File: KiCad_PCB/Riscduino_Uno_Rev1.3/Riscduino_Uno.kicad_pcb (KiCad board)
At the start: 2 copper layers, 68.8 x 53.6 mm, 87 parts, among them J10 Conn_01x06_Pin, J11 USB_B_Micro, J12 Conn_01x08_Pin, J13 Conn_01x10_Pin, J2 Conn_01x03_Pin, J3 Conn_01x01, J4 Conn_02x04_Odd_Even, J5 ISP, J6 Conn_01x01, J7 Conn_01x01, J8 Conn_01x01, J9 Conn_01x08_Pin, SW1 4Pin Round Button SPST Straig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, U2 W25Q32JVSS, U3 23LC1024-I/P, U4 W25Q32JVSS, U5 Riscduino, U6 LM1117MP-3.3, U7 LM1117S-ADJ, U8 CH340C, X1 ASE-10.000MHZ-LC-T

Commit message: Update
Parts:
- added R19: 0E, Riscduino:R_0603_1608Metric_Pad0.98x0.95mm_HandSolder, B.Cu at (119.2, 88.7)
- added R25: 0E, Riscduino:R_0603_1608Metric_Pad0.98x0.95mm_HandSolder, B.Cu at (119.2, 90.2)
- C15: moved to B.Cu
- C16: renamed from C17; moved to B.Cu
- C17: renamed from C18; moved to B.Cu
- C23: renamed from C10; moved to B.Cu
- C24: renamed from C12; moved to B.Cu
- R13: renamed from R14; moved to B.Cu
- R26: renamed from R15; moved to B.Cu
- R27: renamed from R16; moved to B.Cu
- moved R15 21.8 mm to (111.7, 59.6)
- moved C3 21.7 mm to (133.9, 50.8), turned to 180 degrees
- moved D2 19.0 mm to (111.5, 61.4), turned to 180 degrees
- moved J7 16.1 mm to (122.7, 66.6), turned to 90 degrees
- moved C20 14.5 mm to (135.1, 66.5), turned to 90 degrees
- moved C15 12.6 mm to (132.9, 66.5), turned to 90 degrees
- moved C26 11.5 mm to (130.2, 93.9)
- moved JP2 9.30 mm to (124.3, 75.0)
- moved C25 8.30 mm to (130.1, 90.2), turned to -90 degrees
- moved R24 8.06 mm to (119.2, 94.0), turned to 180 degrees
- moved C17 5.29 mm to (126.4, 65.2), turned to 180 degrees
- moved U5 4.21 mm to (125.0, 88.0)
- moved J5 3.85 mm to (117.9, 61.8)
- moved J4 3.53 mm to (118.1, 57.8)
- moved R12 3.47 mm to (127.3, 55.8), turned to 90 degrees
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- renumbered C6 to C10, C8 to C11, C14 to C12, C16 to C13, C19 to C14, C22 to C18, C21 to C19, C23 to C20, C24 to C21, C25 to C22, C20 to C25, C7 to C5, C9 to C6, C11 to C7, C13 to C8, C5 to C9, D3 to D2, D1 to D3, J5 to J1, J13 to J10, J2 to J11, J7 to J12, J10 to J2, J9 to J3, J6 to J4, J3 to J5, J4 to J6, J8 to J7, J11 to J8, J12 to J9, JP2 to JP1, JP1 to JP2, R2 to R1, R12 to R10, R5 to R11, R32 to R12, R19 to R14, R23 to R15, R20 to R16, R21 to R17, R22 to R18, R4 to R2, R25 to R20, R27 to R21, R29 to R22, R28 to R23, R33 to R24, R24 to R28, R26 to R29, R6 to R3, R7 to R4, R3 to R5, R9 to R6, R8 to R7, R13 to R8, R11 to R9, U4 to U1, U3 to U2, U5 to U3, U6 to U4, U8 to U5, U7 to U6, U2 to U7
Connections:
- J10 pad 8: mprj_io_12 -> mprj_io_30
- U5 pad 2: ardunio_d0 -> Net-(U5-TXD)
- U5 pad 3: ardunio_d1 -> Net-(U5-RXD)
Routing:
- net ardunio_d3: track 124.0 -> 63.5 mm, vias 5 -> 1
- net mprj_io_12: track 87.0 -> 35.3 mm, vias 5 -> 3
- net ardunio_d2: track 120.7 -> 70.1 mm, vias 5 -> 1
- net +3.3V: track 358.2 -> 397.8 mm, vias 14 -> 8
- net CARAVEL_FLASH_IO0: track 81.9 -> 112.5 mm
- net ardunio_d4: track 84.9 -> 55.2 mm, vias 2 -> 1
- net mprj_io_30: track 0.00 -> 27.8 mm, vias 0 -> 2
- net ardunio_d0: track 102.1 -> 79.3 mm, vias 6 -> 2
- net USER_SRAM_SSN: track 88.2 -> 65.7 mm, vias 3 -> 4
- net USER_FLASH_IO2: track 80.3 -> 99.7 mm, vias 2 -> 3
- net +5VP: track 13.9 -> 33.2 mm, vias 1 -> 0
- net Net-(U6-ADJ): track 14.4 -> 33.1 mm
- net ardunio_a1: track 71.4 -> 53.3 mm, vias 6 -> 1
- net USER_FLASH_IO3: track 100.6 -> 118.3 mm, vias 4 -> 3
- net ISP_SSN: track 64.8 -> 48.5 mm, vias 3 -> 0
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
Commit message: Power Supervisory Circuit
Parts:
- added C28: 0.1uf, Riscduino.Library:C_0603_1608Metric_Pad1.08x0.95mm_HandSolder, B.Cu at (128.3, 51.7)
- added U8: APX811, Package_TO_SOT_SMD:SOT-143_Handsoldering, B.Cu at (133.1, 51.8)
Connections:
- C3 pad 1: ~{RST} -> ~{MR}
- R1 pad 2: ~{RST} -> ~{MR}
- R12 pad 2: ~{RST} -> ~{MR}
- SW1 pad 2: ~{RST} -> ~{MR}
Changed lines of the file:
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@@
   (net 82 "unconnected-(U5-~{RTS}-Pad14)")
   (net 83 "unconnected-(U5-R232-Pad15)")
+  (net 84 "~{MR}")
   (footprint "Connector_PinHeader_2.54mm:PinHeader_1x01_P2.54mm_Vertical" (layer "F.Cu")
     (at 118.1354 57.8358 180)
@@
       (net 4 "+3.3V") (pintype "passive"))
     (pad "2" smd roundrect (at 0.9125 0) (size 1.1 0.95) (layers "F.Cu" "F.Paste" "F.Mask") (roundrect_rratio 0.25)
-      (net 14 "~{RST}") (pintype "passive"))
+      (net 84 "~{MR}") (pintype "passive"))
     (model "${KICAD6_3DMODEL_DIR}/Resistor_SMD.3dshapes/R_0603_1608Metric.wrl"
       (offset (xyz 0 0 0))
@@
       (stroke (width 0.1) (type solid)) (layer "F.Fab"))
     (pad "1" smd roundrect (at -1.0375 0 180) (size 1.175 1.45) (layers "F.Cu" "F.Paste" "F.Mask") (roundrect_rratio 0.2127659574)
-      (net 14 "~{RST}") (pintype "passive"))
+      (net 84 "~{MR}") (pintype "passive"))
     (pad "2" smd roundrect (at 1.0375 0 180) (size 1.175 1.45) (layers "F.Cu" "F.Paste" "F.Mask") (roundrect_rratio 0.2127659574)
       (net 2 "GND") (pintype "passive"))
@@
       (net 2 "GND") (pinfunction "1") (pintype "passive"))
     (pad "2" smd rect (at -2.88 2 180) (size 2.75 1) (layers "F.Cu" "F.Paste" "F.Mask")
-      (net 14 "~{RST}") (pinfunction "2") (pintype "passive"))
+      (net 84 "~{MR}") (pinfunction "2") (pintype "passive"))
     (pad "2" smd rect (at 2.88 2 180) (size 2.75 1) (layers "F.Cu" "F.Paste" "F.Mask")
-      (net 14 "~{RST}") (pinfunction "2") (pintype "passive"))
+      (net 84 "~{MR}") (pinfunction "2") (pintype "passive"))
     (model "${KICAD6_3DMODEL_DIR}/Button_Switch_SMD.3dshapes/SW_SPST_EVPBF.wrl"
       (offset (xyz 0 0 0))
@@
       (net 80 "Net-(C26-Pad2)") (pintype "passive"))
     (pad "2" smd roundrect (at 0.9125 0 90) (size 1.1 0.95) (layers "B.Cu" "B.Paste" "B.Mask") (roundrect_rratio 0.25)
-      (net 14 "~{RST}") (pintype "passive"))
+      (net 84 "~{MR}") (pintype "passive"))
     (model "${KICAD6_3DMODEL_DIR}/Resistor_SMD.3dshapes/R_0603_1608Metric.wrl"
       (offset (xyz 0 0 0))
@@
     )
   )
+  (footprint "Riscduino.Library:C_0603_1608Metric_Pad1.08x0.95mm_HandSolder" (layer "B.Cu")
+    (at 128.27 51.6625 -90)
+    (descr "Capacitor SMD 0603 (1608 Metric), square (rectangular) end terminal, IPC_7351 nominal with elongated pad for handsoldering. (Body size source: IPC-SM-782 page 76, https://www.pcb-3d.com/wordpress/wp-content/uploads/ipc-sm-782a_amendment_1_and_2.pdf), generated with kicad-footprint-generator")
+    (tags "capacitor handsolder")
+    (property "Sheetfile" "Riscduino_Uno.kicad_sch")
+    (property "Sheetname" "")
+    (property "ki_description" "Unpolarized capacitor")
+    (property "ki_keywords" "cap capacitor")
+    (attr smd)
+    (fp_text reference "C28" (at -0.2036 -1.2446 90) (layer "B.SilkS")
+        (effects (font (size 1.016 1.016) (thickness 0.1524)) (justify mirror))
+    )
+    (fp_text value "0.1uf" (at 0 -1.43 90) (layer "B.Fab") hide
+        (effects (font (size 1 1) (thickness 0.15)) (justify mirror))
+    )
+    (fp_text user "${REFERENCE}" (at 0 0 90) (layer "B.Fab") hide
+        (effects (font (size 0.4 0.4) (thickness 0.06)) (justify mirror))
+    )
+    (fp_line (start -0.146267 -0.51) (end 0.146267 -0.51)
+      (stroke (width 0.12) (type solid)) (layer "B.SilkS"))
+    (fp_line (start -0.146267 0.51) (end 0.146267 0.51)
+      (stroke (width 0.12) (type solid)) (layer "B.SilkS"))
+    (fp_line (start -1.65 -0.73) (end -1.65 0.73)
+      (stroke (width 0.05) (type solid)) (layer "B.CrtYd"))
+    (fp_line (start -1.65 0.73) (end 1.65 0.73)
+      (stroke (width 0.05) (type solid)) (layer "B.CrtYd"))
+    (fp_line (start 1.65 -0.73) (end -1.65 -0.73)
+      (stroke (width 0.05) (type solid)) (layer "B.CrtYd"))
+    (fp_line (start 1.65 0.73) (end 1.65 -0.73)
+      (stroke (width 0.05) (type solid)) (layer "B.CrtYd"))
+    (fp_line (start -0.8 -0.4) (end -0.8 0.4)
+      (stroke (width 0.1) (type solid)) (layer "B.Fab"))
+    (fp_line (start -0.8 0.4) (end 0.8 0.4)
+      (stroke (width 0.1) (type solid)) (layer "B.Fab"))
+    (fp_line (start 0.8 -0.4) (end -0.8 -0.4)
+      (stroke (width 0.1) (type solid)) (layer "B.Fab"))
+    (fp_line (start 0.8 0.4) (end 0.8 -0.4)
+      (stroke (width 0.1) (type solid)) (layer "B.Fab"))
+    (pad "1" smd roundrect (at -0.8625 0 270) (size 1.075 0.95) (layers "B.Cu" "B.Paste" "B.Mask") (roundrect_rratio 0.25)
+      (net 4 "+3.3V") (pintype "passive"))
+    (pad "2" smd roundrect (at 0.8625 0 270) (size 1.075 0.95) (layers "B.Cu" "B.Paste" "B.Mask") (roundrect_rratio 0.25)
+      (net 2 "GND") (pintype "passive"))
+    (model "${KICAD6_3DMODEL_DIR}/Capacitor_SMD.3dshapes/C_0603_1608Metric.wrl"
+      (offset (xyz 0 0 0))
+      (scale (xyz 1 1 1))
+      (rotate (xyz 0 0 0))
+    )
+  )
   (footprint "Riscduino.Library:R_0603_1608Metric_Pad0.98x0.95mm_HandSolder" (layer "B.Cu")
     (at 87.3252 85.2189 -90)
@@
       (offset (xyz 0 0 0))
       (scale (xyz 1 1 1))
+      (rotate (xyz 0 0 0))
+    )
+  )
+  (footprint "Package_TO_SOT_SMD:SOT-143_Handsoldering" (layer "B.Cu")
+    (at 133.096 51.816 180)
+    (descr "SOT-143 Handsoldering https://www.nxp.com/docs/en/package-information/SOT143B.pdf")
+    (tags "SOT-143 Handsoldering")
+    (property "Sheetfile" "Riscduino_Uno.kicad_sch")
+    (property "Sheetname" "")
+    (property "ki_description" "Power supply supervisor, Manual reset, Threshold 3.08V, SOT-143")
+    (property "ki_keywords" "Supervisor Reset")
+    (attr smd)
+    (fp_text reference "U8" (at -3.556 0 90) (layer "B.SilkS")
+        (effects (font (size 1 1) (thickness 0.15)) (justify mirror))
+    )
+    (fp_text value "APX811" (at -0.02 -2.48) (layer "B.Fab")
+        (effects (font (size 1 1) (thickness 0.15)) (justify mirror))
+    )
+    (fp_text user "${REFERENCE}" (at 0 0 90) (layer "B.Fab")
+        (effects (font (size 0.5 0.5) (thickness 0.075)) (justify mirror))
+    )
+    (fp_line (start -0.65 -1.56) (end 0.65 -1.56)
+      (stroke (width 0.12) (type solid)) (layer "B.SilkS"))
+    (fp_line (start 0.65 1.56) (end -2.35 1.56)
+      (stroke (width 0.12) (type solid)) (layer "B.SilkS"))
+    (fp_line (start -2.6 -1.7) (end -2.6 1.7)
+      (stroke (width 0.05) (type solid)) (layer "B.CrtYd"))
+    (fp_line (start -2.6 -1.7) (end 2.6 -1.7)
+      (stroke (width 0.05) (type solid)) (layer "B.CrtYd"))
+    (fp_line (start 2.6 1.7) (end -2.6 1.7)
+      (stroke (width 0.05) (type solid)) (layer "B.CrtYd"))
+    (fp_line (start 2.6 1.7) (end 2.6 -1.7)
+      (stroke (width 0.05) (type solid)) (layer "B.CrtYd"))
+    (fp_line (start -0.65 -1.45) (end -0.65 0.95)
+      (stroke (width 0.1) (type solid)) (layer "B.Fab"))
+    (fp_line (start -0.65 0.95) (end -0.15 1.45)
+      (stroke (width 0.1) (type solid)) (layer "B.Fab"))
+    (fp_line (start -0.15 1.45) (end 0.65 1.45)
+      (stroke (width 0.1) (type solid)) (layer "B.Fab"))
+    (fp_line (start 0.65 -1.45) (end -0.65 -1.45)
+      (stroke (width 0.1) (type solid)) (layer "B.Fab"))
+    (fp_line (start 0.65 1.45) (end 0.65 -1.45)
+      (stroke (width 0.1) (type solid)) (layer "B.Fab"))
+    (pad "1" smd rect (at -1.5 0.75 180) (size 1.7 1) (layers "B.Cu" "B.Paste" "B.Mask")
+      (net 2 "GND") (pinfunction "GND") (pintype "power_in"))
+    (pad "2" smd rect (at -1.5 -0.95 180) (size 1.7 0.6) (layers "B.Cu" "B.Paste" "B.Mask")
+      (net 14 "~{RST}") (pinfunction "~{RESET}") (pintype "output"))
+    (pad "3" smd rect (at 1.5 -0.95 180) (size 1.7 0.6) (layers "B.Cu" "B.Paste" "B.Mask")
+      (net 84 "~{MR}") (pinfunction "~{MR}") (pintype "input"))
+    (pad "4" smd rect (at 1.5 0.95 180) (size 1.7 0.6) (layers "B.Cu" "B.Paste" "B.Mask")
+      (net 4 "+3.3V") (pinfunction "VCC") (pintype "power_in"))
+    (model "${KICAD6_3DMODEL_DIR}/Package_TO_SOT_SMD.3dshapes/SOT-143.wrl"
+      (offset (xyz 0 0 0))
+      (scale (xyz 1 1 1))

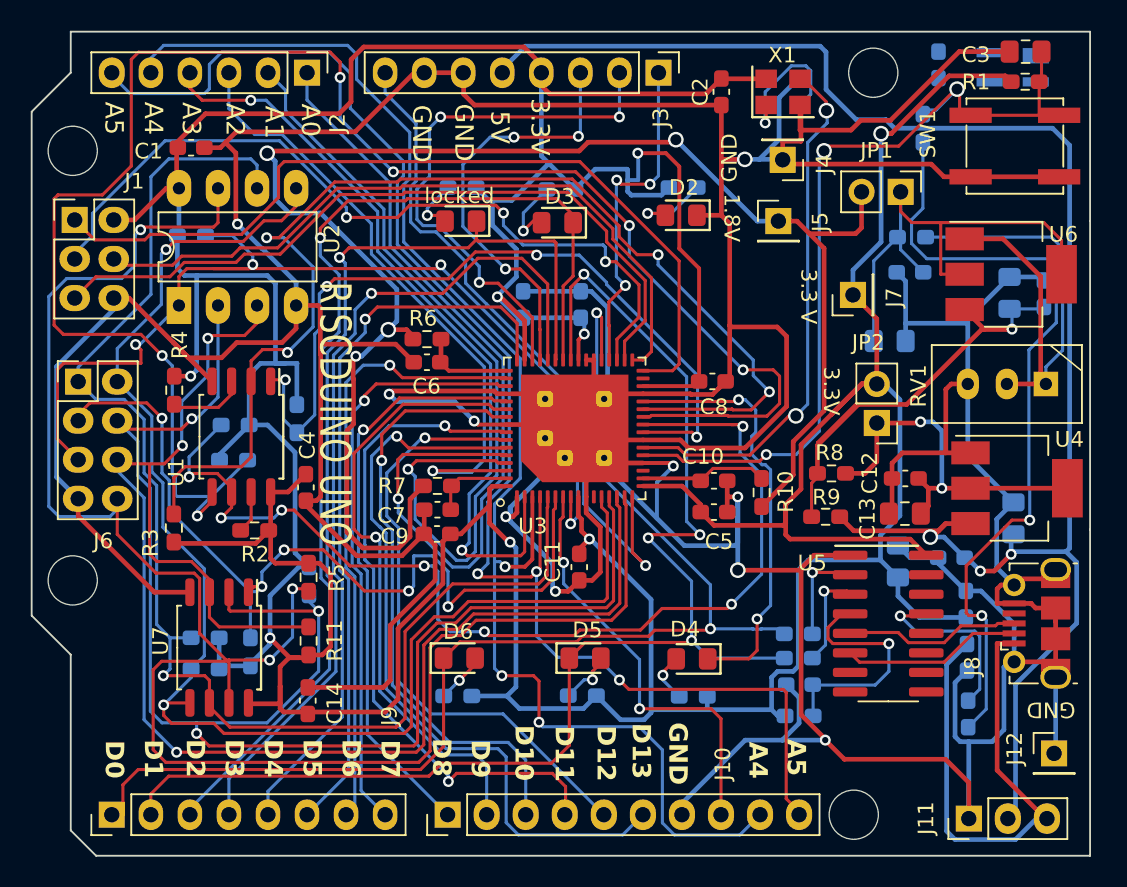
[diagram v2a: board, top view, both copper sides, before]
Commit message: 1.3 Uno Schematic update
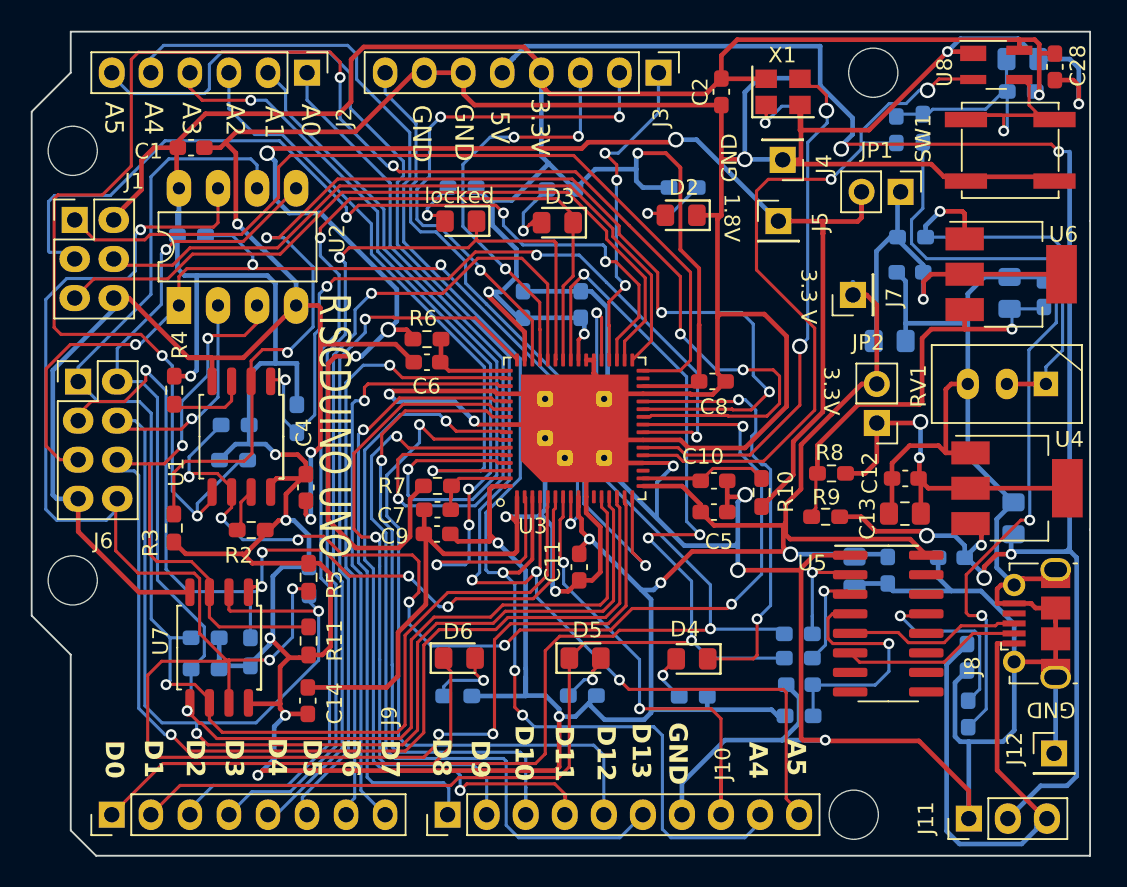
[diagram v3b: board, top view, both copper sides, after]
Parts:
- added R32: 0E-DNI, Riscduino:C_0603_1608Metric_Pad1.08x0.95mm_HandSolder, B.Cu at (125.5, 55.9)
- C28: moved to F.Cu
- C3, R1: moved to B.Cu
- U8: value APX811 -> APX811-29UG-7; moved to F.Cu
- moved C28 7.57 mm to (135.8, 51.8)
- moved C22 5.54 mm to (125.0, 84.5), turned to -90 degrees
- moved C16 2.91 mm to (122.8, 84.7), turned to -90 degrees
- moved U8 1.08 mm to (132.0, 51.7), turned to 0 degrees
- moved R1 0.68 mm to (133.7, 53.4), turned to 180 degrees
- moved C3 0.52 mm to (133.7, 51.3), turned to 0 degrees
- moved SW1 0.41 mm to (132.9, 57.2)
- moved R2 0.23 mm to (83.6, 81.9)
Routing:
- net ~{MR}: track 0.00 -> 27.9 mm, vias 0 -> 1
- net GND: track 486.3 -> 509.0 mm, vias 10 -> 14
- net /+1.8VP: track 32.9 -> 25.1 mm, vias 0 -> 1
- net ardunio_d0: track 79.3 -> 86.1 mm
- net Net-(U6-ADJ): track 33.1 -> 26.4 mm, vias 0 -> 1
- net ~{RST}: track 55.0 -> 48.7 mm, vias 3 -> 2
- net +3.3V: track 397.8 -> 403.9 mm, vias 8 -> 15
- net ardunio_a1: track 53.3 -> 47.3 mm
- net ardunio_a0: track 55.1 -> 49.2 mm
- net ardunio_d12: track 39.6 -> 45.3 mm
- net Net-(X1-EN): track 9.64 -> 4.37 mm
- net +5V: track 108.7 -> 113.7 mm, vias 3 -> 6
- net ardunio_a3: track 50.3 -> 55.2 mm, vias 2 -> 4
- net ISP_SCK: track 52.0 -> 56.9 mm
- net ardunio_d11: track 43.0 -> 47.3 mm
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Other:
- board text added: "Riscduino Uno Rev 1.3 Sept 2023"
- board text removed: "Riscduino Uno Rev 1.3 August 2023"

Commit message: Riscduino Uno 1.3
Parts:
- renumbered C9 to C10, C10 to C11, C3 to C15, C15 to C16, C16 to C17, C17 to C18, C18 to C19, C19 to C20, C20 to C21, C21 to C22, C22 to C23, C23 to C24, C24 to C25, C25 to C26, C26 to C27, C27 to C28, C28 to C3, C11 to C5, C5 to C8, C8 to C9, J2 to J1, J1 to J2, R2 to R1, R11 to R10, R32 to R11, R1 to R13, R13 to R15, R17 to R16, R16 to R17, R15 to R18, R18 to R19, R4 to R2, R19 to R20, R20 to R21, R23 to R22, R22 to R23, R21 to R24, R24 to R25, R25 to R26, R26 to R27, R27 to R28, R28 to R29, R29 to R32, R5 to R4, R6 to R5, R7 to R6, R8 to R7, R9 to R8, R10 to R9, U8 to U1, U1 to U2, U2 to U3, U3 to U4, U4 to U5, U5 to U6, U6 to U7, U7 to U8
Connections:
- U4 pad 57: ardunio_d11 -> ardunio_d12
- U4 pad 58: ardunio_d12 -> ardunio_d11
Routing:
- net ardunio_d11: track 47.3 -> 42.9 mm, vias 2 -> 1
- net ardunio_d12: track 45.3 -> 49.0 mm, vias 1 -> 2
- net GND: track 509.0 -> 510.8 mm
- net +3.3V: track 403.9 -> 402.6 mm
- net ardunio_d0: track 86.1 -> 87.3 mm
- net ardunio_a2: track 41.8 -> 43.0 mm
- net Net-(D3-A): track 6.21 -> 5.12 mm
- net ISP_SCK: track 56.9 -> 57.8 mm
- net ardunio_d1: track 87.8 -> 88.7 mm
- net USER_FLASH_IO2: track 99.4 -> 100.2 mm
- net ardunio_a3: track 55.2 -> 55.9 mm
- net CARAVEL_FLASH_IO1: track 78.5 -> 79.2 mm
- net Net-(D2-A): track 4.95 -> 5.64 mm
- net USER_SRAM_SSN: track 64.1 -> 64.7 mm
- net gpio: track 28.0 -> 27.4 mm
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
